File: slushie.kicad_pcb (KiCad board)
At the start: 2 copper layers, 99.1 x 99.1 mm, 103 parts, among them SW1 SPST, SW2 SPST, SW3 SPST, U1 LM2575, U2 LPC1769 LPCXpresso

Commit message: clean
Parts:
- removed C2: CP, SMD_Packages:SMD-2512_Pol
- removed D5: LED, LEDs:LED-0805
- removed L1: 330µH, Inductors:SELF-WE-PD-XXL
- removed the Nylon Only at (132.7, 149.2)
- removed the Nylon Only at (132.7, 57.8)
- removed the Nylon Only at (224.2, 57.8)
- removed the Nylon Only at (224.2, 149.2)
- removed POWER1: BARREL_JACK, Connect:BARREL_JACK
- removed WINGPWR1, WINGPWR2, WINGPWR3, WINGPWR4: WINGPWR, Connect:bornier2
- added BOOT1: CONN_2, Pin_Headers:Pin_Header_Straight_1x02, F.Cu at (171.6, 82.8)
- added LED1: CONN_2, Pin_Headers:Pin_Header_Straight_1x02, F.Cu at (175.4, 124.7)
- added LED2: CONN_2, Pin_Headers:Pin_Header_Straight_1x02, F.Cu at (175.4, 122.2)
- added LED3: CONN_2, Pin_Headers:Pin_Header_Straight_1x02, F.Cu at (175.4, 119.6)
- added LED4: CONN_2, Pin_Headers:Pin_Header_Straight_1x02, F.Cu at (175.4, 117.1)
- added Nylon Only: 3-1mm, Local:MountingHole_3-1mm, F.Cu at (224.9, 58.7)
- added Nylon Only: 3-1mm, Local:MountingHole_3-1mm, F.Cu at (133.5, 58.7)
- added Nylon Only: 3-1mm, Local:MountingHole_3-1mm, F.Cu at (133.5, 150.1)
- added Nylon Only: 3-1mm, Local:MountingHole_3-1mm, F.Cu at (224.9, 150.1)
- added P1: CONN_1, Local:TabRA, F.Cu at (139.8, 141.2)
- added P2: CONN_1, Local:TabRA, F.Cu at (147.4, 141.2)
- added PAUSE1: CONN_2, Pin_Headers:Pin_Header_Straight_1x02, F.Cu at (171.6, 80.3)
- added RESET1: CONN_2, Pin_Headers:Pin_Header_Straight_1x02, F.Cu at (171.6, 85.3)
- C1: value CP -> 22µF; footprint SMD_Packages:SMD-2512_Pol -> Capacitors_ThroughHole:Capacitor5x11RM2.5
- C10, C11, C12, C13, C3, C4, C5, C6, C7, C8, C9: footprint SMD_Packages:SMD-0805 -> Local:0805C
- C14, C15, C16, C17, C18, C19: footprint SMD_Packages:SMD-0805 -> Local:EIA3216
- D1: value 1N5818 -> LED; footprint Diodes_SMD:Diode-Universal-SMB-SMC_Handsoldering -> Local:0805LED
- D2: footprint LEDs:LED-0805 -> 0805LED
- D3, D4: footprint LEDs:LED-0805 -> Local:0805LED
- END1, END2, END3, END4, END5, END6, END7, END8: footprint Pin_Headers:Pin_Header_Straight_1x03 -> Local:Pin_Header_Right_Angle_1x03
- ETHERNET1: footprint Connect:RJ45_TRANSFO -> Local:MJF12T3L-KF06B3YG-0808
- R1, R10, R11, R12, R13, R14, R15, R16, R17, R18, R19, R2, R20, R21, R22, R23, R24, R25, R26, R27, R28, R29, R3, R30, R31, R32, R33, R34, R35, R36, R37, R38, R39, R4, R40, R5, R6, R7, R8, R9: footprint Resistors_SMD:Resistor_SMD0805_HandSoldering -> Local:0805R
- SD1: footprint SD:MICRO_SD_HINGE_AMP -> MICRO_SD
- SW1, SW2, SW3: footprint Discret:SW_PUSH_SMALL -> Local:Tactswitch
- TH1, TH2, TH3, TH4, TH5, TH6: footprint Pin_Headers:Pin_Header_Straight_1x02 -> Local:Pin_Header_Angled_2x01
- U1: value LM2575 -> TR05S; footprint SMD_Packages:TO-263-5 -> Local:TR05S
- U2: footprint LPCXpresso_boards.mod:LPCXPRESSO_LPC1769 -> LPCXPRESSO_LPC1769
- USB1: footprint Connect:USB_MINI_B -> Local:USB_MICRO_B
- WING1, WING2: footprint Pin_Headers:Pin_Header_Angled_2x04 -> Socket_Strips:Socket_Strip_Angled_2x04
- WING3, WING4: footprint Pin_Headers:Pin_Header_Angled_2x08 -> Socket_Strips:Socket_Strip_Angled_2x08
- moved U2 140.6 mm to (213.5, 150.1), turned to 90 degrees
- moved R10 112.7 mm to (143.6, 59.9), turned to 90 degrees
- moved I2C1 112.1 mm to (141.1, 62.5), turned to 90 degrees
- moved SPI1 109.5 mm to (217.3, 65.0), turned to 90 degrees
- moved R12 108.8 mm to (214.8, 66.3), turned to 270 degrees
- moved SD1 108.0 mm to (202.1, 152.7), turned to 180 degrees
- moved USB1 106.1 mm to (156.3, 153.9), turned to 0 degrees
- moved R11 104.9 mm to (143.6, 65.0), turned to 270 degrees
- moved C3 103.7 mm to (162.6, 148.6)
- moved WING4 103.3 mm to (223.5, 129.5), turned to 270 degrees
- moved R13 102.4 mm to (209.7, 66.3), turned to 270 degrees
- moved WING1 102.0 mm to (134.7, 129.5), turned to 90 degrees
- moved WING3 102.0 mm to (223.6, 79.6), turned to 270 degrees
- moved END1 101.6 mm to (212.2, 70.1), turned to 90 degrees
- moved R20 101.4 mm to (214.8, 71.4), turned to 270 degrees
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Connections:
- net +24V renamed Net-(C1-Pad1)
- D1 pad 1: GND -> Net-(D1-Pad1)
- D1 pad 2: Net-(D1-Pad2) -> GND
- R31 pad 2: Net-(D2-Pad1) -> Net-(D1-Pad1)
- R32 pad 2: Net-(D3-Pad1) -> Net-(D2-Pad1)
- R33 pad 2: Net-(D4-Pad1) -> Net-(D3-Pad1)
- R34 pad 2: Net-(D5-Pad1) -> Net-(D4-Pad1)
- U1 pad 2: Net-(D1-Pad2) -> GND
- U1 pad 3: GND -> +3.3V
- U2 pad 42: /PWM1 -> /PWM2
- U2 pad 43: /PWM2 -> /PWM1
- U2 pad 48: /END4 -> /END7
- U2 pad 49: /END5 -> /END6
- U2 pad 50: /END6 -> /END5
- U2 pad 52: /END7 -> /END4
- WING1 pad 1: /PWM2 -> (no net)
- WING1 pad 2: /PWM1 -> /PWM0
- WING1 pad 3: /SDA -> GND
- WING1 pad 4: /SCL -> +3.3V
- WING1 pad 5: GND -> /SCL
- WING1 pad 6: +3.3V -> /SDA
- WING1 pad 7: (no net) -> /PWM1
- WING1 pad 8: /PWM0 -> /PWM2
- WING2 pad 1: /PWM5 -> (no net)
- WING2 pad 2: /PWM4 -> /PWM3
- WING2 pad 3: /SDA -> +3.3V
- WING2 pad 4: /SCL -> +3.3V
- WING2 pad 5: +3.3V -> /SCL
- WING2 pad 6: +3.3V -> /SDA
- WING2 pad 7: (no net) -> /PWM4
- WING2 pad 8: /PWM3 -> /PWM5
- WING3 pad 1: /EN3 -> /EN0
- WING3 pad 10: +3.3V -> /SCL
- WING3 pad 11: /DIR1 -> /STP2
- WING3 pad 12: /EN1 -> /EN2
- WING3 pad 13: /STP1 -> /DIR2
- WING3 pad 14: /DIR0 -> /STP3
- WING3 pad 15: /EN0 -> /EN3
- WING3 pad 16: /STP0 -> /DIR3
- WING3 pad 2: /DIR3 -> /STP0
- WING3 pad 3: /DIR2 -> /STP1
- WING3 pad 4: /STP3 -> /DIR0
- WING3 pad 5: /STP2 -> /DIR1
- WING3 pad 6: /EN2 -> /EN1
- WING3 pad 7: /SDA -> GND
- WING3 pad 8: /SCL -> +3.3V
- WING3 pad 9: GND -> /SDA
- WING4 pad 1: /EN7 -> /EN4
- WING4 pad 10: +3.3V -> /SCL
- WING4 pad 11: /DIR5 -> /STP6
- WING4 pad 12: /EN5 -> /EN6
- WING4 pad 13: /STP5 -> /DIR6
- WING4 pad 14: /DIR4 -> /STP7
- WING4 pad 15: /EN4 -> /EN7
- WING4 pad 16: /STP4 -> /DIR7
- WING4 pad 2: /DIR7 -> /STP4
- WING4 pad 3: /DIR6 -> /STP5
- WING4 pad 4: /STP7 -> /DIR4
- WING4 pad 5: /STP6 -> /DIR5
- WING4 pad 6: /EN6 -> /EN5
- WING4 pad 7: /SDA -> +3.3V
- WING4 pad 8: /SCL -> +3.3V
- WING4 pad 9: +3.3V -> /SDA
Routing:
- net GND: track 534.2 -> 130.6 mm, vias 53 -> 3
- net Net-(C1-Pad1): track 225.0 -> 42.5 mm, vias 1 -> 0
- net +3.3V: track 613.5 -> 468.6 mm, vias 6 -> 1
- net /RESET: track 16.6 -> 98.0 mm
- net /LED4: track 126.6 -> 70.7 mm, vias 1 -> 0
- net /TX: track 60.9 -> 10.5 mm
- net /RX: track 60.1 -> 10.5 mm
- net /PAUSE: track 66.1 -> 28.5 mm, vias 1 -> 0
- net /LED3: track 41.2 -> 3.78 mm
- net /SCL: track 298.9 -> 266.8 mm, vias 3 -> 0
- net /BOOT: track 72.5 -> 40.9 mm, vias 1 -> 0
- net /LED2: track 34.7 -> 3.78 mm
- net /TH4: track 95.4 -> 68.4 mm
- net /SDA: track 276.1 -> 302.3 mm, vias 1 -> 0
- net /TH3: track 88.5 -> 62.9 mm
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- removed copper zone on F.Cu, net GND
- removed copper zone on F.Cu, net Net-(C3-Pad1)
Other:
- outline, holes or cut-outs redrawn
- net class Default: trace_width 0.4318 -> 0.4
- board text added: "GND"
- board text added: "MOSI"
- board text added: "Slushie v0.0.1 ©2014 b@Zi.iS CERN OHL v1.2"
- board text removed: "+"
- board text removed: "-"
- board text removed: "LED1"
- board text removed: "LED2"
- board text removed: "LED3"
- board text removed: "LED4"
- board text removed: "LPC1769 LPCXpresso"
- board text removed: "MOSi"
- board text removed: "R31:4"
- board text removed: "v0.0.1 Slushie ©2014 b@Zi.iS CERN OHL v.1.2"

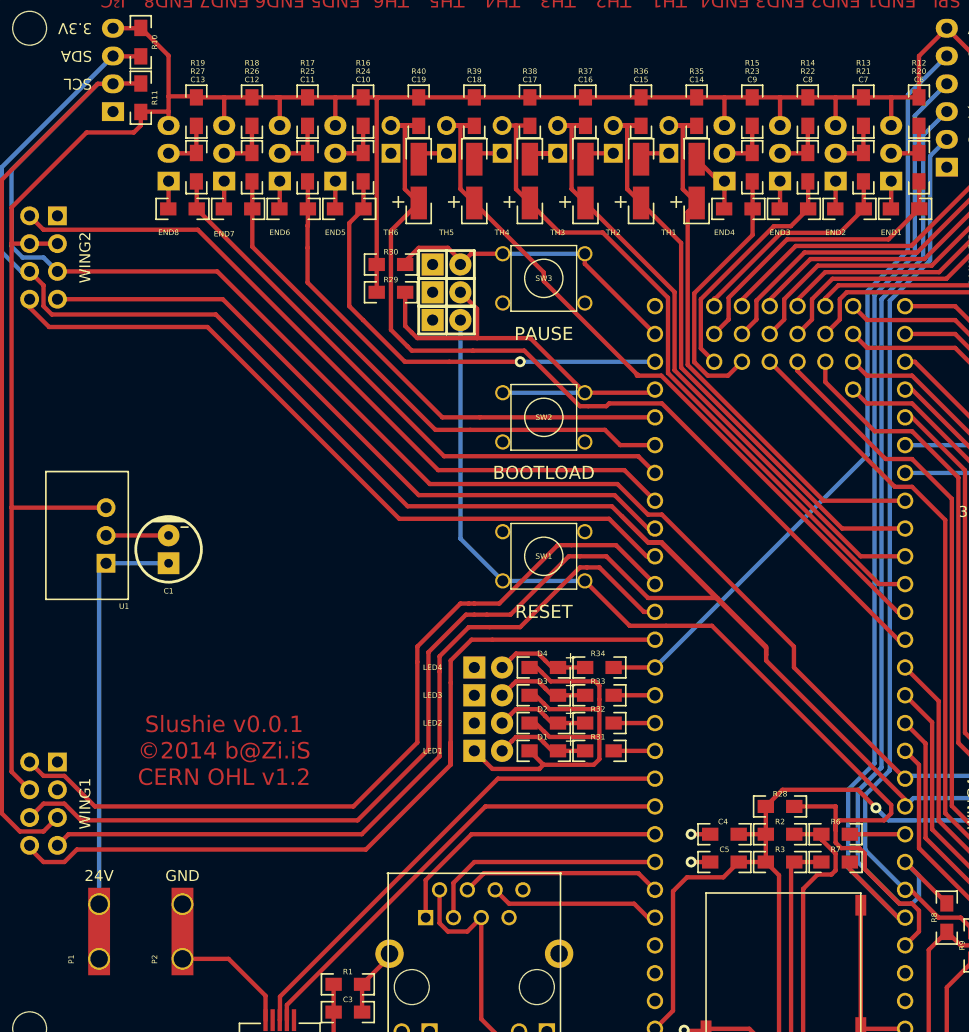
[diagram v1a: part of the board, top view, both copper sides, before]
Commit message: need to enbigen silk
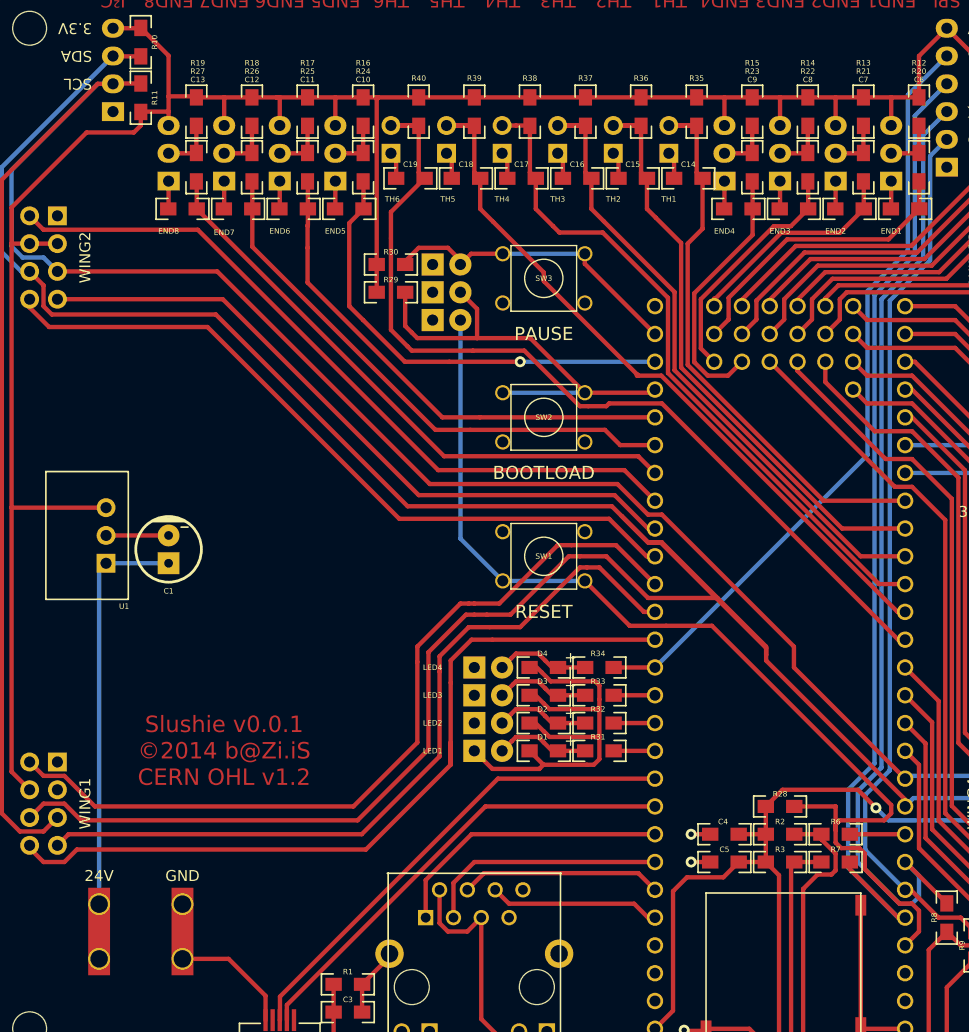
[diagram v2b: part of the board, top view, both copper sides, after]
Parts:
- C14, C15, C16, C17, C18, C19: footprint Local:EIA3216 -> Local:0805C
- D2: footprint 0805LED -> Local:0805LED
- ETHERNET1: footprint Local:MJF12T3L-KF06B3YG-0808 -> MJF12T3L-KF06B3YG-0808
- SD1: footprint MICRO_SD -> Local:MICRO_SD
- U2: footprint LPCXPRESSO_LPC1769 -> Local:LPCXPRESSO_LPC1769
- moved C14 0.80 mm to (193.7, 72.4), turned to 180 degrees
- moved C15 0.80 mm to (188.6, 72.4), turned to 180 degrees
- moved C16 0.80 mm to (183.5, 72.4), turned to 180 degrees
- moved C17 0.80 mm to (178.4, 72.4), turned to 180 degrees
- moved C18 0.80 mm to (173.4, 72.4), turned to 180 degrees
- moved C19 0.80 mm to (168.3, 72.4), turned to 180 degrees
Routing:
- net GND: track 130.6 -> 126.4 mm
- net /TH3: track 62.9 -> 62.3 mm
- net /TH1: track 55.8 -> 55.3 mm
- net /TH4: track 68.4 -> 67.9 mm
- net /TH2: track 59.5 -> 58.9 mm
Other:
- rule pad_to_mask_clearance: 0.2 -> 0

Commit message: more titdy
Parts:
- removed Nylon Only: 3-1mm, Local:MountingHole_3-1mm (x4)
- added M1: CONN_1, Local:MountingHole_3-1mm, F.Cu at (133.5, 150.1)
- added M2: CONN_1, Local:MountingHole_3-1mm, F.Cu at (224.9, 150.1)
- added M3: CONN_1, Local:MountingHole_3-1mm, F.Cu at (133.5, 58.7)
- added M4: CONN_1, Local:MountingHole_3-1mm, F.Cu at (224.9, 58.7)
- ETHERNET1: footprint MJF12T3L-KF06B3YG-0808 -> Local:MJF12T3L-KF06B3YG-0808
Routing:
- net GND: track 126.4 -> 120.7 mm
- net Net-(C1-Pad1): track 42.5 -> 43.4 mm
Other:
- net class Default: clearance 0.2 -> 0.4; via_drill 0.5 -> 0.4
- rule trace_clearance: 0.2 -> 0.4

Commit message: fixes
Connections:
- ETHERNET1 pad 1: /TD+ -> /RD+
- ETHERNET1 pad 2: +3.3V -> /RD-
- ETHERNET1 pad 3: /TD- -> +3.3V
- ETHERNET1 pad 4: /RD+ -> GND
- ETHERNET1 pad 5: +3.3V -> GND
- ETHERNET1 pad 6: /RD- -> +3.3V
- ETHERNET1 pad 7: (no net) -> /TD+
- ETHERNET1 pad 8: GND -> /TD-
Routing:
- net /RD-: track 15.7 -> 29.1 mm
- net /RD+: track 18.4 -> 29.3 mm
- net /D-: track 42.5 -> 52.7 mm
- net /LED4: track 70.7 -> 80.6 mm
- net /TD+: track 26.1 -> 18.4 mm
- net /D+: track 44.7 -> 52.3 mm
- net /TD-: track 22.4 -> 18.8 mm
- net /SCK: track 89.0 -> 92.3 mm
- net /TH4: track 67.9 -> 70.8 mm
- net GND: track 120.7 -> 122.4 mm
- net /END1: track 20.9 -> 19.3 mm
- net +3.3V: track 468.6 -> 467.2 mm
- net /END2: track 22.0 -> 21.0 mm
- net /END0: track 27.2 -> 26.2 mm
- net /EN1: track 20.5 -> 19.5 mm
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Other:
- net class Default: clearance 0.4 -> 0.2
- rule trace_clearance: 0.4 -> 0.2
- board text added: "Slushie v0.0.2 ©2014 b@Zi.iS CERN OHL v1.2"
- board text removed: "Slushie v0.0.1 ©2014 b@Zi.iS CERN OHL v1.2"
